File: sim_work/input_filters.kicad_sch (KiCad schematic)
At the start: 64 parts

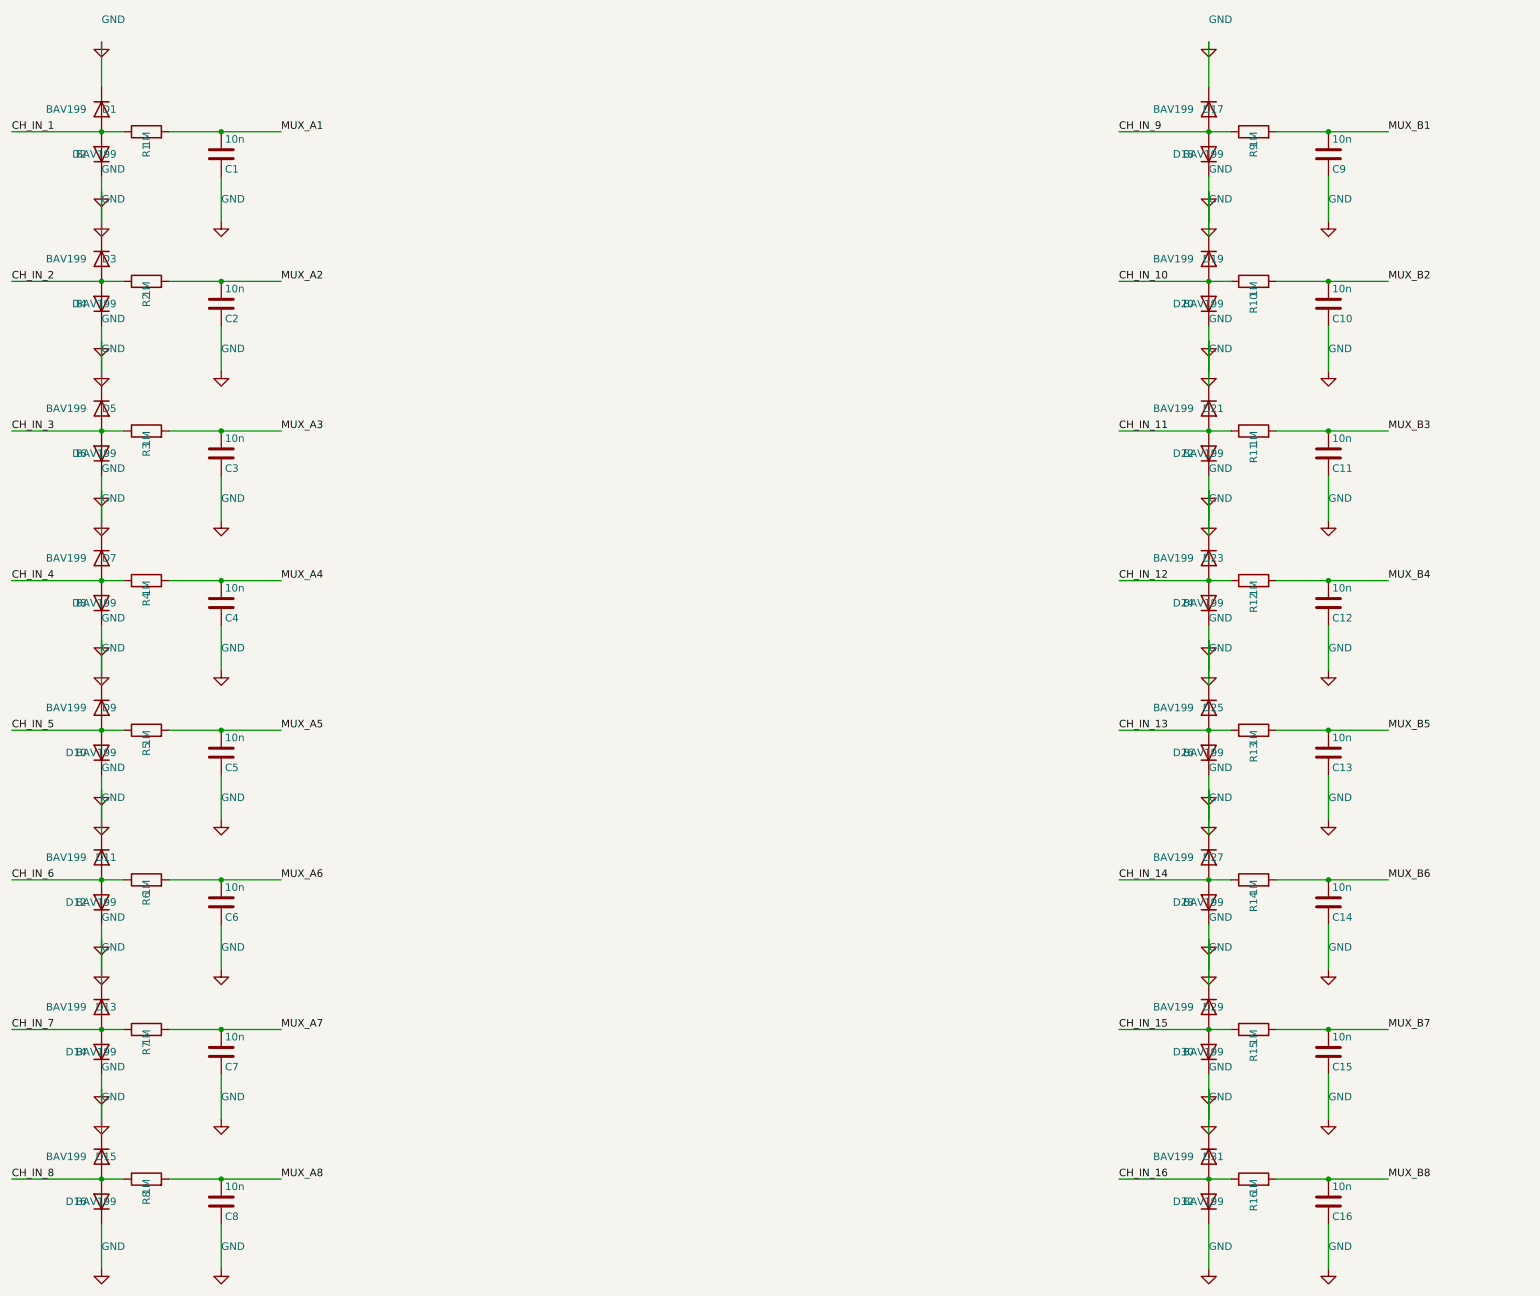
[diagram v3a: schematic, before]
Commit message: Add comparison mode, fix SimGUI subprocess popups, DAC7800 IC boxes
- SimGUI: fix Python path detection (FindPython searches Python312/313/311)
- SimGUI: suppress console popup windows (CREATE_NO_WINDOW for subprocess)
- SimGUI: add Comparison project (MDAC vs Analog oscillator side-by-side)
- SimGUI: fix async wrapping (direct await instead of Task.Run)
- Pipeline: draw DAC7800 as proper IC box with pin labels (VREF/IOUT/VCTRL)
- Pipeline: fix electrometer_362 layout (spacing, junction dots at T-junctions)
- Pipeline: fix summing amp gain annotations (BP=-0.455, not -2.2)
- Pipeline: add analog_osc command for friend's SVF oscillator simulation
- Docs: comparison_guide.md, updated README and PROJECT tracker

Co-Authored-By: Claude Opus 4.6 <noreply@anthropic.com>
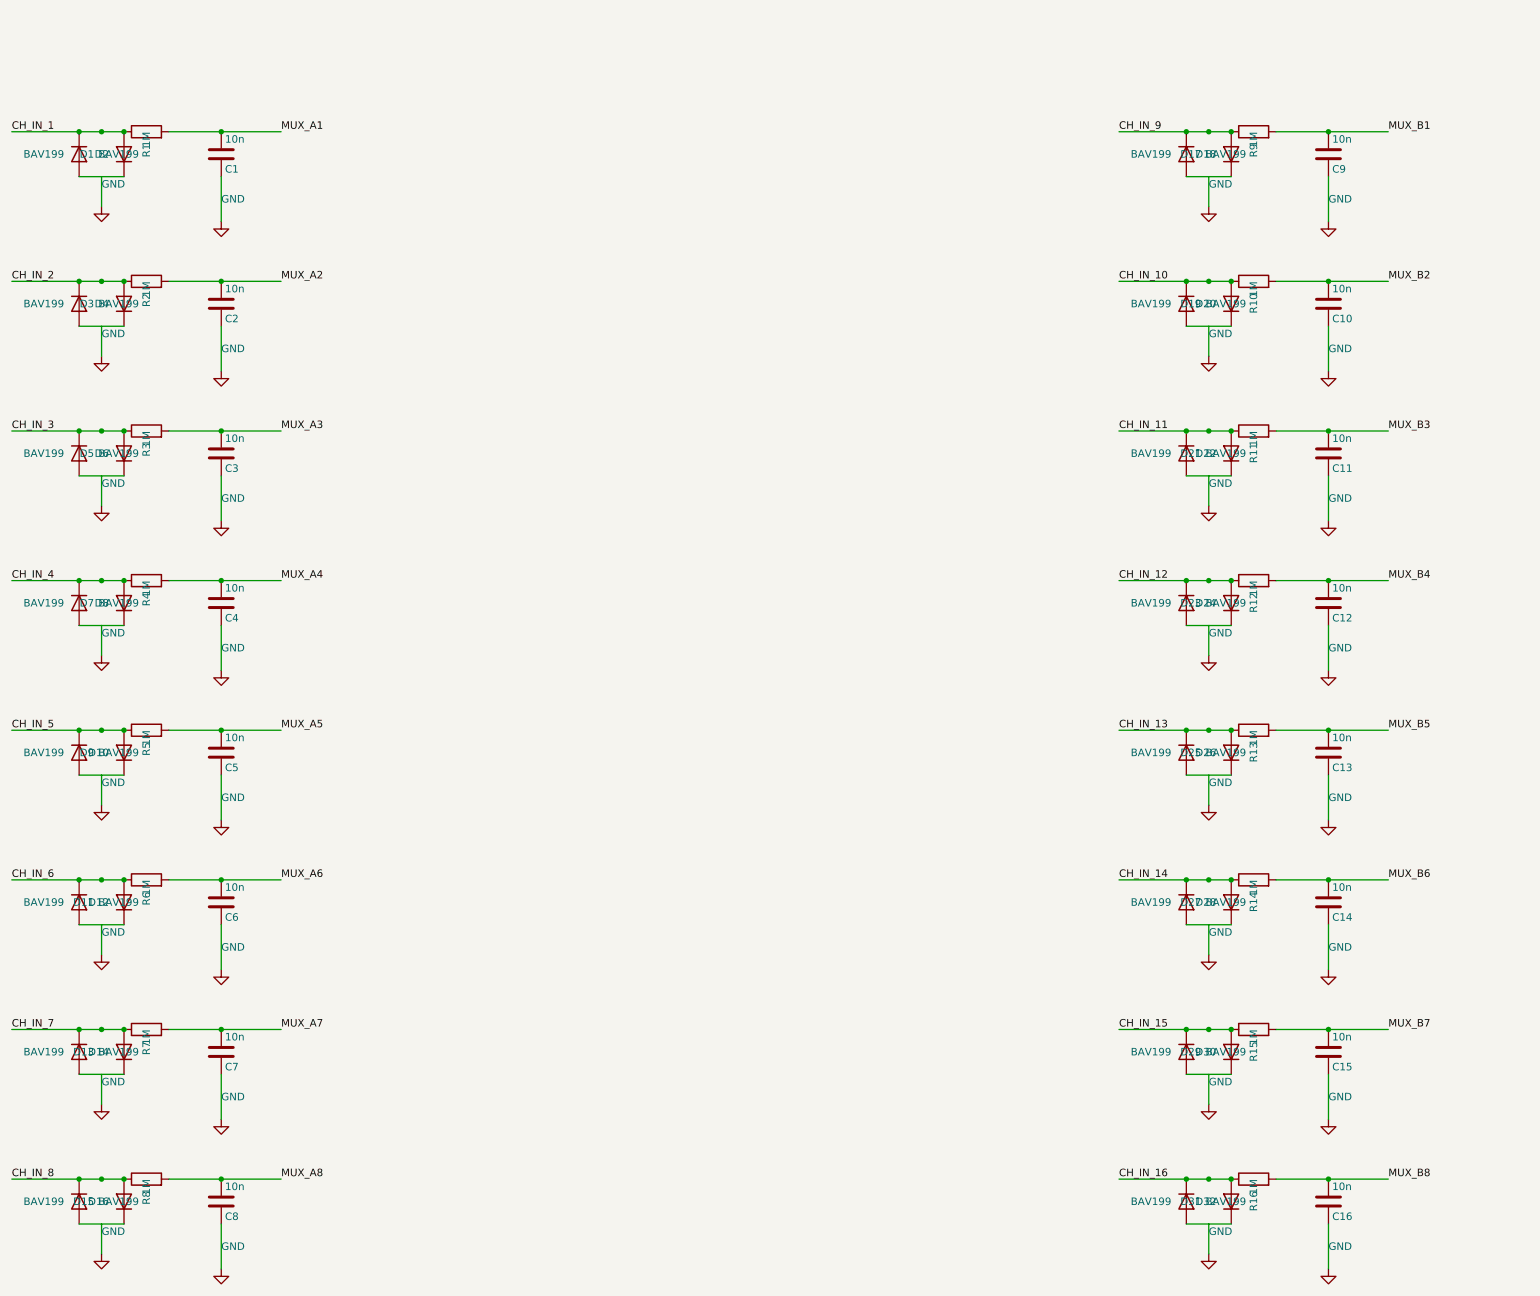
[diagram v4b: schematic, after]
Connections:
- net CH_IN_1: now also D1.1 (K); no longer D1.2 (A)
- net CH_IN_10: now also D19.1 (K); no longer D19.2 (A)
- net CH_IN_11: now also D21.1 (K); no longer D21.2 (A)
- net CH_IN_12: now also D23.1 (K); no longer D23.2 (A)
- net CH_IN_13: now also D25.1 (K); no longer D25.2 (A)
- net CH_IN_14: now also D27.1 (K); no longer D27.2 (A)
- net CH_IN_15: now also D29.1 (K); no longer D29.2 (A)
- net CH_IN_16: now also D31.1 (K); no longer D31.2 (A)
- net CH_IN_2: now also D3.1 (K); no longer D3.2 (A)
- net CH_IN_3: now also D5.1 (K); no longer D5.2 (A)
- net CH_IN_4: now also D7.1 (K); no longer D7.2 (A)
- net CH_IN_5: now also D9.1 (K); no longer D9.2 (A)
- net CH_IN_6: now also D11.1 (K); no longer D11.2 (A)
- net CH_IN_7: now also D13.1 (K); no longer D13.2 (A)
- net CH_IN_8: now also D15.1 (K); no longer D15.2 (A)
- net CH_IN_9: now also D17.1 (K); no longer D17.2 (A)
- net GND: no longer D1.1 (K), D10.1 (K), D11.1 (K), D12.1 (K), D13.1 (K), D14.1 (K), D15.1 (K), D16.1 (K), D17.1 (K), D18.1 (K), D19.1 (K), D2.1 (K), D20.1 (K), D21.1 (K), D22.1 (K), D23.1 (K), D24.1 (K), D25.1 (K), D26.1 (K), D27.1 (K), D28.1 (K), D29.1 (K), D3.1 (K), D30.1 (K), D31.1 (K), D32.1 (K), D4.1 (K), D5.1 (K), D6.1 (K), D7.1 (K), D8.1 (K), D9.1 (K)
- new net: D23.2 (A), D24.1 (K)
- new net: D15.2 (A), D16.1 (K)
- new net: D17.2 (A), D18.1 (K)
- new net: D5.2 (A), D6.1 (K)
- new net: D31.2 (A), D32.1 (K)
- new net: D19.2 (A), D20.1 (K)
- new net: D10.1 (K), D9.2 (A)
- new net: D1.2 (A), D2.1 (K)
- new net: D11.2 (A), D12.1 (K)
- new net: D7.2 (A), D8.1 (K)
- new net: D13.2 (A), D14.1 (K)
- new net: D25.2 (A), D26.1 (K)
- new net: D3.2 (A), D4.1 (K)
- new net: D27.2 (A), D28.1 (K)
- new net: D29.2 (A), D30.1 (K)
- new net: D21.2 (A), D22.1 (K)
